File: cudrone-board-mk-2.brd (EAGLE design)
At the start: 100 x 70 mm, 42 parts, among them Q1 BSS138, U1 EDISON_CONNECTOR_FULLMOUNTING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, U2 FTS31XS-U, U4 TPS62065

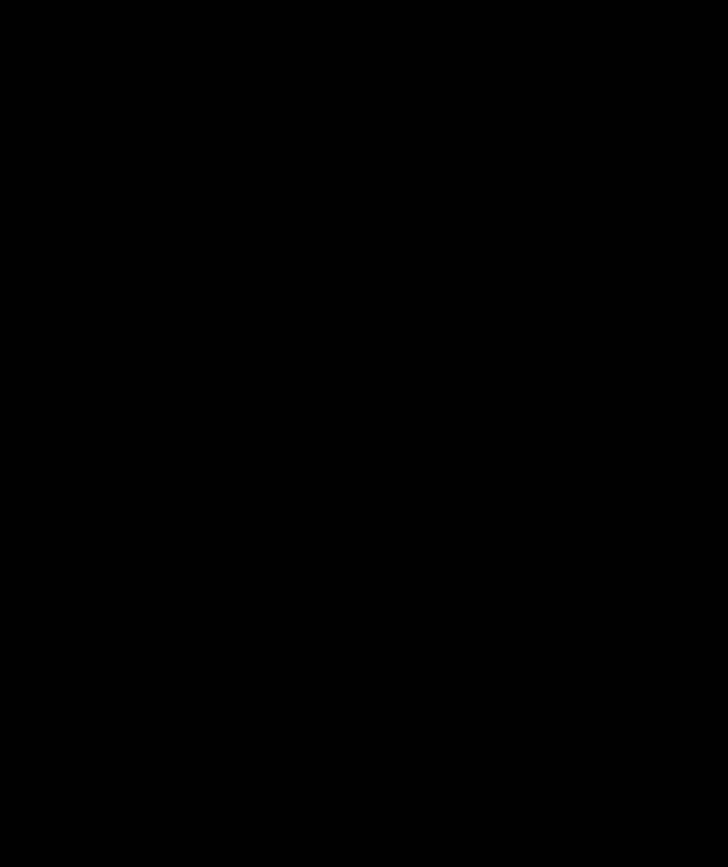
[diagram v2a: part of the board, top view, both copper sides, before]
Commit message: Added sd card
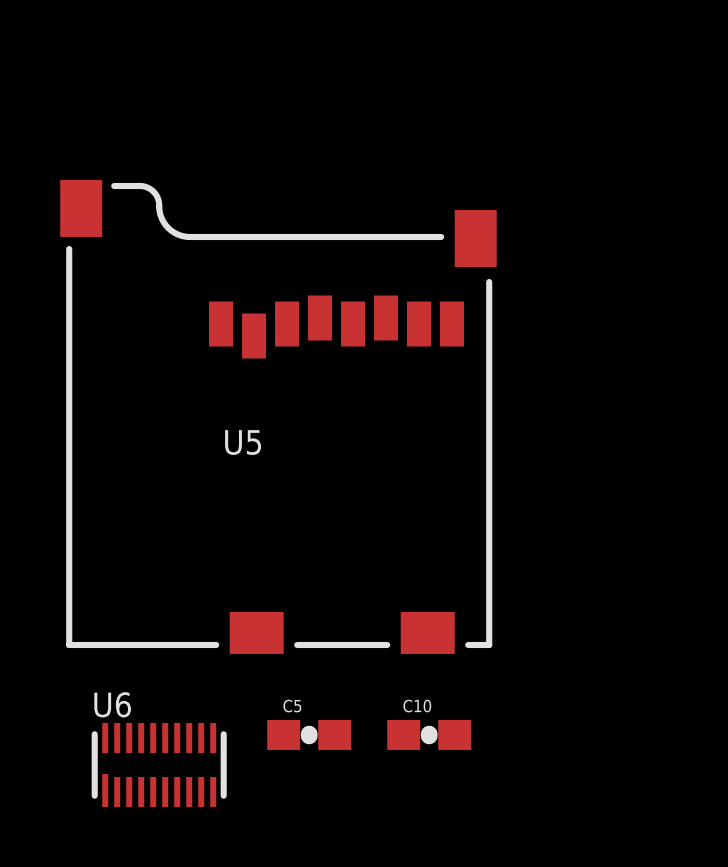
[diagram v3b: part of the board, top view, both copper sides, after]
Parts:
- added C10, C5: 0.1uF, SparkFun-Capacitors:0603-CAP
- added U5: USD-SOCKETNEW, SparkFun-Connectors:MICRO-SD-SOCKET-PP
- added U6: TXB0108, Testing:UFDFN-20
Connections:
- new net N$20: U5.1, U6.P$20
- new net N$21: U5.2, U6.P$19
- new net N$22: U5.3, U6.P$18
- new net N$23: U5.7, U6.P$14
- new net N$24: U5.8, U6.P$13
- new net SCK: U5.5, U6.P$12, U6.P$17
- net 1.8V: now also C5.1, U6.P$5, U6.P$6
- net 3.3V: now also C10.1, U5.4, U6.P$16
- net GND: now also C10.2, C5.2, U5.6, U5.GND1, U5.GND3, U6.P$15
- net GP77_SD_0_CD#: now also U5.CD1
- net GP78_SD_0_CLK: now also U6.P$4
- net GP79_SD_0_CMD: now also U6.P$3
- net GP80_SD_0_DAT0: now also U6.P$7
- net GP81_SD_0_DAT1: now also U6.P$8
- net GP82_SD_0_DAT2: now also U6.P$1
- net GP83_SD_0_DAT3: now also U6.P$2
- net GP84_SD_CLK_FB: now also U6.P$9
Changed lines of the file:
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@@
 <attribute name="PROD_ID" value="RES-07828" x="-88" y="-150" size="1.778" layer="27" display="off"/>
+</element>
+<element name="U5" library="SparkFun-Connectors" package="MICRO-SD-SOCKET-PP" value="USD-SOCKETNEW" x="-62" y="-175"/>
+<element name="U6" library="Testing" package="UFDFN-20" value="TXB0108" x="-73" y="-179"/>
+<element name="C5" library="SparkFun-Capacitors" package="0603-CAP" value="0.1uF" x="-68" y="-178">
+<attribute name="PROD_ID" value="CAP-00810" x="-95" y="-156" size="1.778" layer="27" display="off"/>
+</element>
+<element name="C10" library="SparkFun-Capacitors" package="0603-CAP" value="0.1uF" x="-64" y="-178">
+<attribute name="PROD_ID" value="CAP-00810" x="-95" y="-159" size="1.778" layer="27" display="off"/>
 </element>
 </elements>
@@
 <contactref element="R10" pad="1"/>
 <contactref element="R12" pad="1"/>
-<wire x1="-66.85" y1="-152" x2="-74.85" y2="-152" width="0" layer="19" extent="1-1"/>
+<contactref element="U5" pad="GND3"/>
+<contactref element="U5" pad="GND1"/>
+<contactref element="U5" pad="6"/>
+<contactref element="U6" pad="P$15"/>
+<contactref element="C5" pad="2"/>
+<contactref element="C10" pad="2"/>
+<wire x1="-67.15" y1="-178" x2="-72.8" y2="-178.1" width="0" layer="19" extent="1-1"/>
+<wire x1="-63.15" y1="-178" x2="-67.15" y2="-178" width="0" layer="19" extent="1-1"/>
+<wire x1="-65.44" y1="-164.1" x2="-67.15" y2="-178" width="0" layer="19" extent="1-1"/>
+<wire x1="-62.45" y1="-161.45" x2="-65.44" y2="-164.1" width="0" layer="19" extent="1-1"/>
+<wire x1="-66.85" y1="-152" x2="-62.45" y2="-161.45" width="0" layer="19" extent="1-1"/>
 <wire x1="-65.6" y1="-148" x2="-66.85" y2="-152" width="0" layer="19" extent="1-1"/>
 <wire x1="-68.3" y1="-142.3" x2="-65.6" y2="-148" width="0" layer="19" extent="1-1"/>
 <wire x1="-65" y1="-138.3751" x2="-68.3" y2="-142.3" width="0" layer="19" extent="1-1"/>
+<wire x1="-74.85" y1="-152" x2="-66.85" y2="-152" width="0" layer="19" extent="1-1"/>
+<wire x1="-75.6" y1="-160.45" x2="-74.85" y2="-152" width="0" layer="19" extent="1-1"/>
 <wire x1="-71.05" y1="-124" x2="-65" y2="-138.3751" width="0" layer="19" extent="1-1"/>
 <wire x1="-73.15" y1="-116" x2="-71.05" y2="-124" width="0" layer="19" extent="1-1"/>
@@
 <contactref element="U1" pad="8"/>
 <contactref element="U1" pad="10"/>
-<wire x1="49.57" y1="44.38" x2="49.97" y2="44.38" width="0" layer="19" extent="1-1"/>
+<contactref element="U6" pad="P$16"/>
+<contactref element="U5" pad="4"/>
+<contactref element="C10" pad="1"/>
+<wire x1="-64.85" y1="-178" x2="-73.2" y2="-178.1" width="0" layer="19" extent="1-1"/>
+<wire x1="-67.64" y1="-164.1" x2="-64.85" y2="-178" width="0" layer="19" extent="1-1"/>
+<wire x1="49.57" y1="44.38" x2="-67.64" y2="-164.1" width="0" layer="19" extent="1-1"/>
+<wire x1="49.97" y1="44.38" x2="49.57" y2="44.38" width="0" layer="19" extent="1-1"/>
 </signal>
 <signal name="GP183_PWM3">
@@
 <contactref element="C1" pad="2"/>
 <contactref element="R11" pad="1"/>
+<contactref element="U6" pad="P$5"/>
+<contactref element="U6" pad="P$6"/>
+<contactref element="C5" pad="1"/>
+<wire x1="-72.8" y1="-179.9" x2="-73.2" y2="-179.9" width="0" layer="19" extent="1-1"/>
+<wire x1="-68.85" y1="-178" x2="-72.8" y2="-179.9" width="0" layer="19" extent="1-1"/>
+<wire x1="-70.85" y1="-152" x2="-68.85" y2="-178" width="0" layer="19" extent="1-1"/>
 <wire x1="-67.15" y1="-113" x2="-70.85" y2="-152" width="0" layer="19" extent="1-1"/>
 <wire x1="-64.5875" y1="-101.6797" x2="-67.15" y2="-113" width="0" layer="19" extent="1-1"/>
@@
 <signal name="GP84_SD_CLK_FB">
 <contactref element="U1" pad="44"/>
+<contactref element="U6" pad="P$9"/>
+<wire x1="42.77" y1="44.38" x2="-71.6" y2="-179.9" width="0" layer="19" extent="1-1"/>
 </signal>
 <signal name="GP78_SD_0_CLK">
 <contactref element="U1" pad="58"/>
+<contactref element="U6" pad="P$4"/>
+<wire x1="39.97" y1="44.38" x2="-73.6" y2="-179.9" width="0" layer="19" extent="1-1"/>
 </signal>
 <signal name="GP77_SD_0_CD#">
 <contactref element="U1" pad="60"/>
+<contactref element="U5" pad="CD1"/>
+<wire x1="39.57" y1="44.38" x2="-64.05" y2="-174.6" width="0" layer="19" extent="1-1"/>
 </signal>
 <signal name="GP79_SD_0_CMD">
 <contactref element="U1" pad="62"/>
+<contactref element="U6" pad="P$3"/>
+<wire x1="39.17" y1="44.38" x2="-74" y2="-179.9" width="0" layer="19" extent="1-1"/>
 </signal>
 <signal name="GP80_SD_0_DAT0">
 <contactref element="U1" pad="66"/>
+<contactref element="U6" pad="P$7"/>
+<wire x1="38.37" y1="44.38" x2="-72.4" y2="-179.9" width="0" layer="19" extent="1-1"/>
 </signal>
 <signal name="GP81_SD_0_DAT1">
 <contactref element="U1" pad="70"/>
+<contactref element="U6" pad="P$8"/>
+<wire x1="37.57" y1="44.38" x2="-72" y2="-179.9" width="0" layer="19" extent="1-1"/>
 </signal>
 <signal name="GP82_SD_0_DAT2">
 <contactref element="U1" pad="64"/>
+<contactref element="U6" pad="P$1"/>
+<wire x1="38.77" y1="44.38" x2="-74.8" y2="-179.85" width="0" layer="19" extent="1-1"/>
 </signal>
 <signal name="GP83_SD_0_DAT3">
 <contactref element="U1" pad="68"/>
+<contactref element="U6" pad="P$2"/>
+<wire x1="37.97" y1="44.38" x2="-74.4" y2="-179.9" width="0" layer="19" extent="1-1"/>
 </signal>
 <signal name="FW_RCVR">
@@
 <wire x1="-65" y1="-135.6249" x2="-73.15" y2="-152" width="0" layer="19" extent="1-1"/>
 </signal>
+<signal name="N$20">
+<contactref element="U6" pad="P$20"/>
+<contactref element="U5" pad="1"/>
+<wire x1="-70.94" y1="-164.3" x2="-74.8" y2="-178.1" width="0" layer="19" extent="1-1"/>
+</signal>
+<signal name="N$21">
+<contactref element="U5" pad="2"/>
+<contactref element="U6" pad="P$19"/>
+<wire x1="-69.84" y1="-164.7" x2="-74.4" y2="-178.1" width="0" layer="19" extent="1-1"/>
+</signal>
+<signal name="N$22">
+<contactref element="U6" pad="P$18"/>
+<contactref element="U5" pad="3"/>
+<wire x1="-68.74" y1="-164.3" x2="-74" y2="-178.1" width="0" layer="19" extent="1-1"/>
+</signal>
+<signal name="SCK">
+<contactref element="U6" pad="P$17"/>
+<contactref element="U5" pad="5"/>
+<contactref element="U6" pad="P$12"/>
+<wire x1="-71.6" y1="-178.1" x2="-73.6" y2="-178.1" width="0" layer="19" extent="1-1"/>
+<wire x1="-66.54" y1="-164.3" x2="-71.6" y2="-178.1" width="0" layer="19" extent="1-1"/>
+</signal>
+<signal name="N$23">
+<contactref element="U6" pad="P$14"/>
+<contactref element="U5" pad="7"/>
+<wire x1="-64.34" y1="-164.3" x2="-72.4" y2="-178.1" width="0" layer="19" extent="1-1"/>
+</signal>
+<signal name="N$24">
+<contactref element="U6" pad="P$13"/>
+<contactref element="U5" pad="8"/>
+<wire x1="-63.24" y1="-164.3" x2="-72" y2="-178.1" width="0" layer="19" extent="1-1"/>
+</signal>
 </signals>

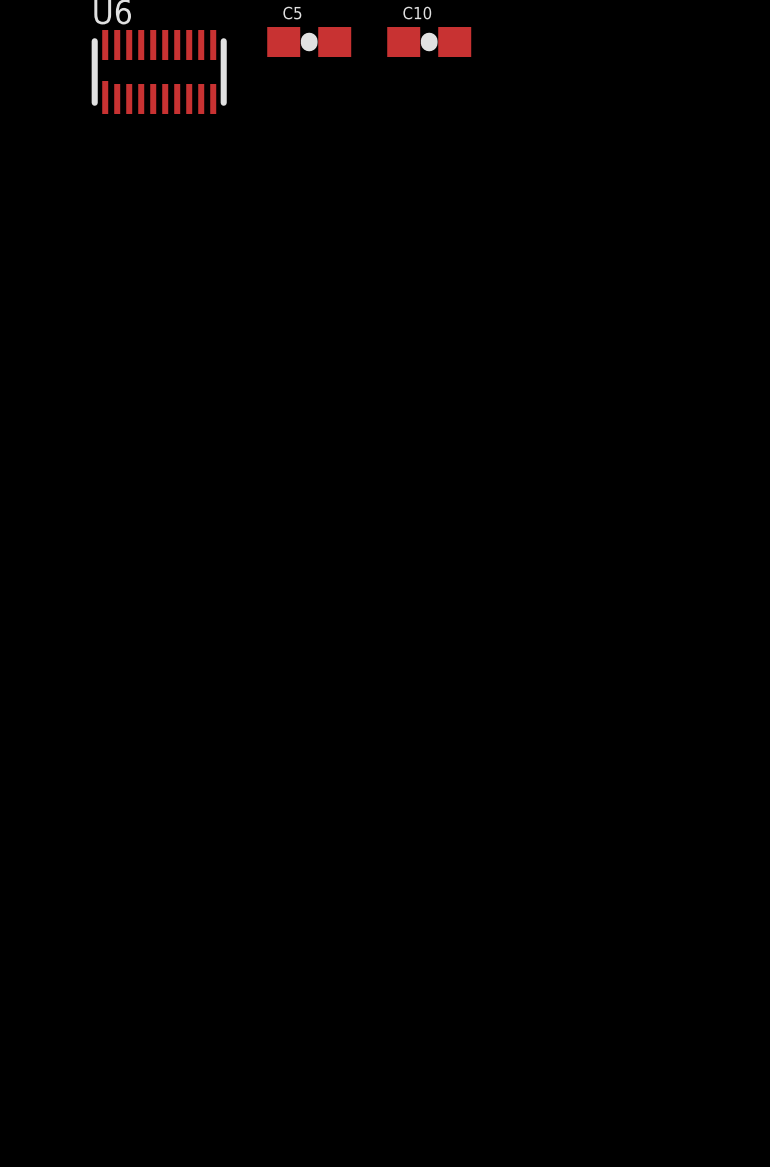
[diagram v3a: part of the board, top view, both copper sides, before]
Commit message: Added the rest of the sparkfun stuff
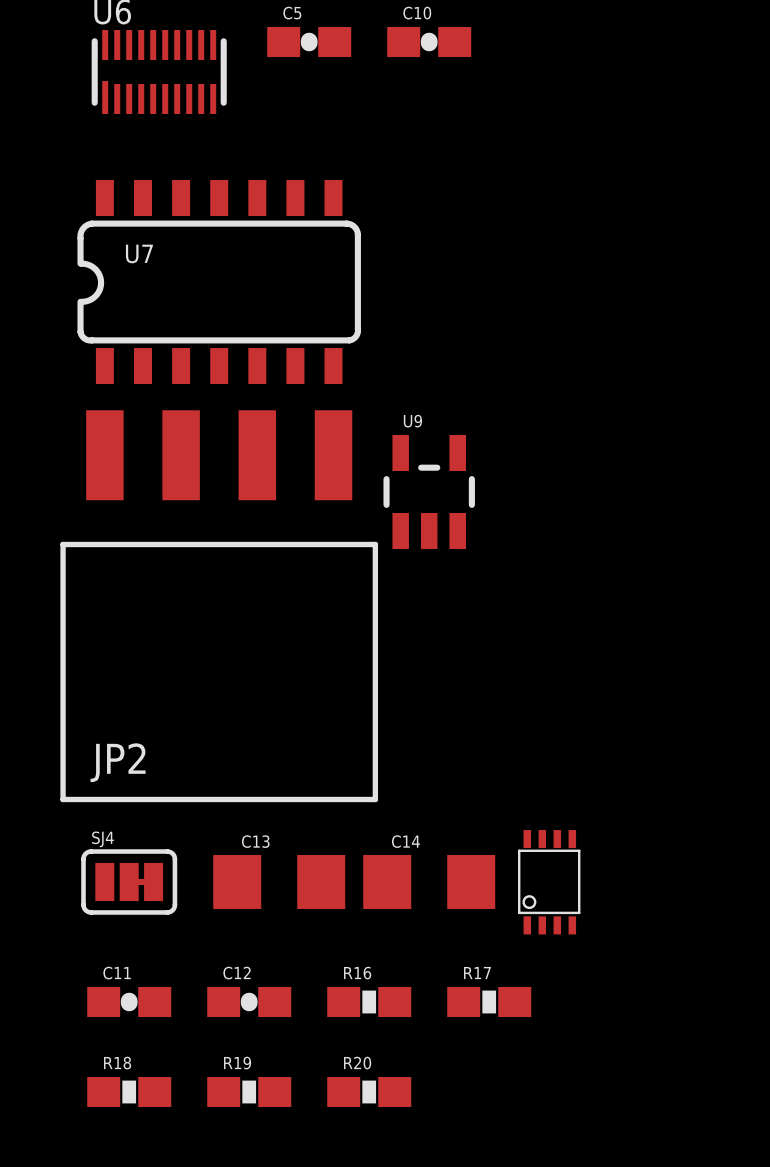
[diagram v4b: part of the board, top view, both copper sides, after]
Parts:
- added C11, C12: 0.1uF, SparkFun-Capacitors:0603-CAP
- added C13, C14: 10uF, SparkFun-Capacitors:1206
- added JP2: (no value), SparkFun-Connectors:1X04_SMD_RA_FEMALE
- added R16, R17: 10K, SparkFun-Resistors:0603-RES
- added R18: 200k, SparkFun-Resistors:0603-RES
- added R19, R20: DNP, SparkFun-Resistors:0603-RES
- added SJ4: Power Select, SparkFun-Passives:PAD-JUMPER-3-2OF3_NC_BY_TRACE_YES_SILK_FULL_BOX
- added U7: (no value), SparkFun-DigitalIC:SO14
- added U8: PCA9306, SparkFun-DigitalIC:PCA9306DC-1:1
- added U9: MIC5205, SparkFun-PowerIC:SOT23-5
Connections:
- new net 3.3V-REGULATED: C14.1, SJ4.3, U9.5
- new net HV_SCL: JP2.1, R17.1, U8.6
- new net HV_SDA: JP2.2, R16.1, U8.5
- new net N$25: R18.1, U8.7, U8.8
- new net UART_1_RX: U7.10
- new net UART_1_TX: U7.11
- new net UART_2_RX: U7.12
- new net UART_2_TX: U7.13
- new net VOUT: C12.1, JP2.3, R16.2, R17.2, R18.2, SJ4.2
- net 1.8V: now also C11.1, R19.2, R20.2, U7.1, U7.8, U8.1
- net 3.3V: now also U7.14
- net GND: now also C11.2, C12.2, C13.2, C14.2, JP2.4, U7.7, U8.4, U9.2
- net GP130_UART_1_RX: now also U7.5
- net GP131_UART_1_TX: now also U7.4
- net GP134_UART_2_RX: now also U7.3
- net GP135_UART_2_TX: now also U7.2
- net GP19_I2C_1_SCL: now also R19.1, U8.2
- net GP20_I2C_1_SDA: now also R20.1, U8.3
- net VSYS: now also C13.1, SJ4.1, U9.1, U9.3
